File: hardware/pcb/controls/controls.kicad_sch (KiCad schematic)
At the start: 52 parts, among them J1 Conn_02x08_Odd_Even, J2 Conn_02x08_Odd_Even, J3 Conn_02x08_Odd_Even, J4 Conn_02x08_Odd_Even, SW1 SW_SPST, SW10 SW_SPST, SW11 SW_SPST, SW12 SW_SPST, SW2 SW_SPST, SW3 SW_SPST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

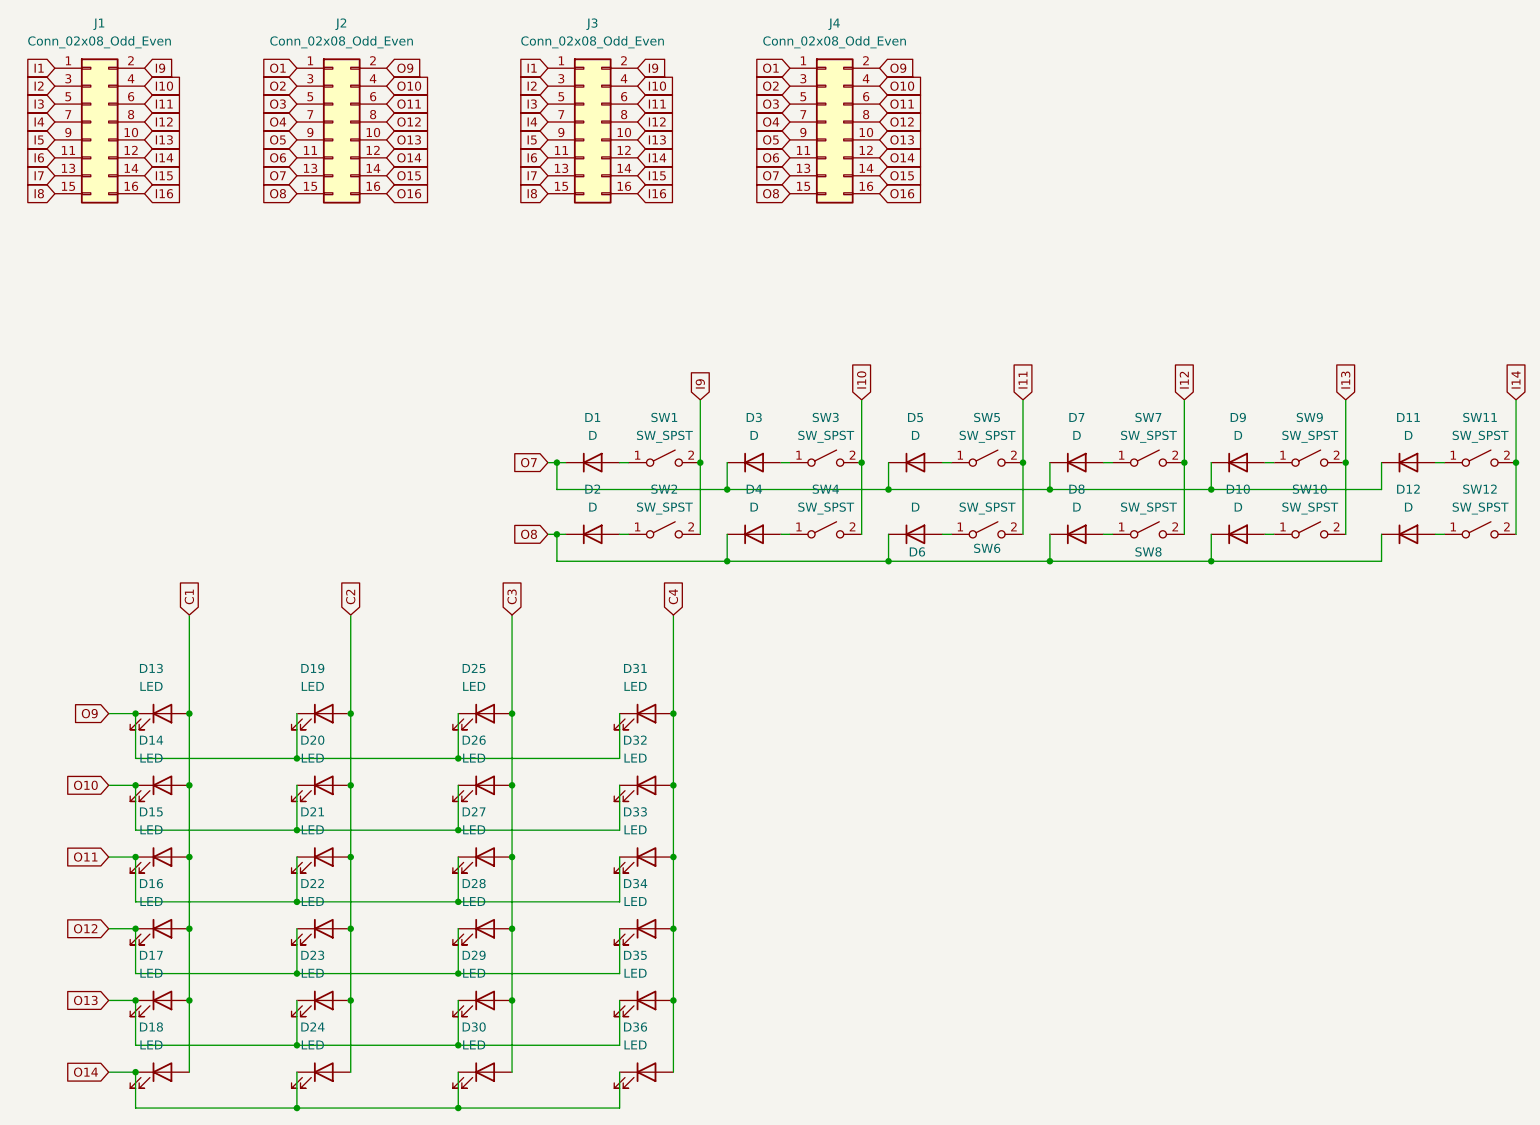
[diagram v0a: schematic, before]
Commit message: hardware: add schematics
add controls, io, keys, and nucleo hat boards
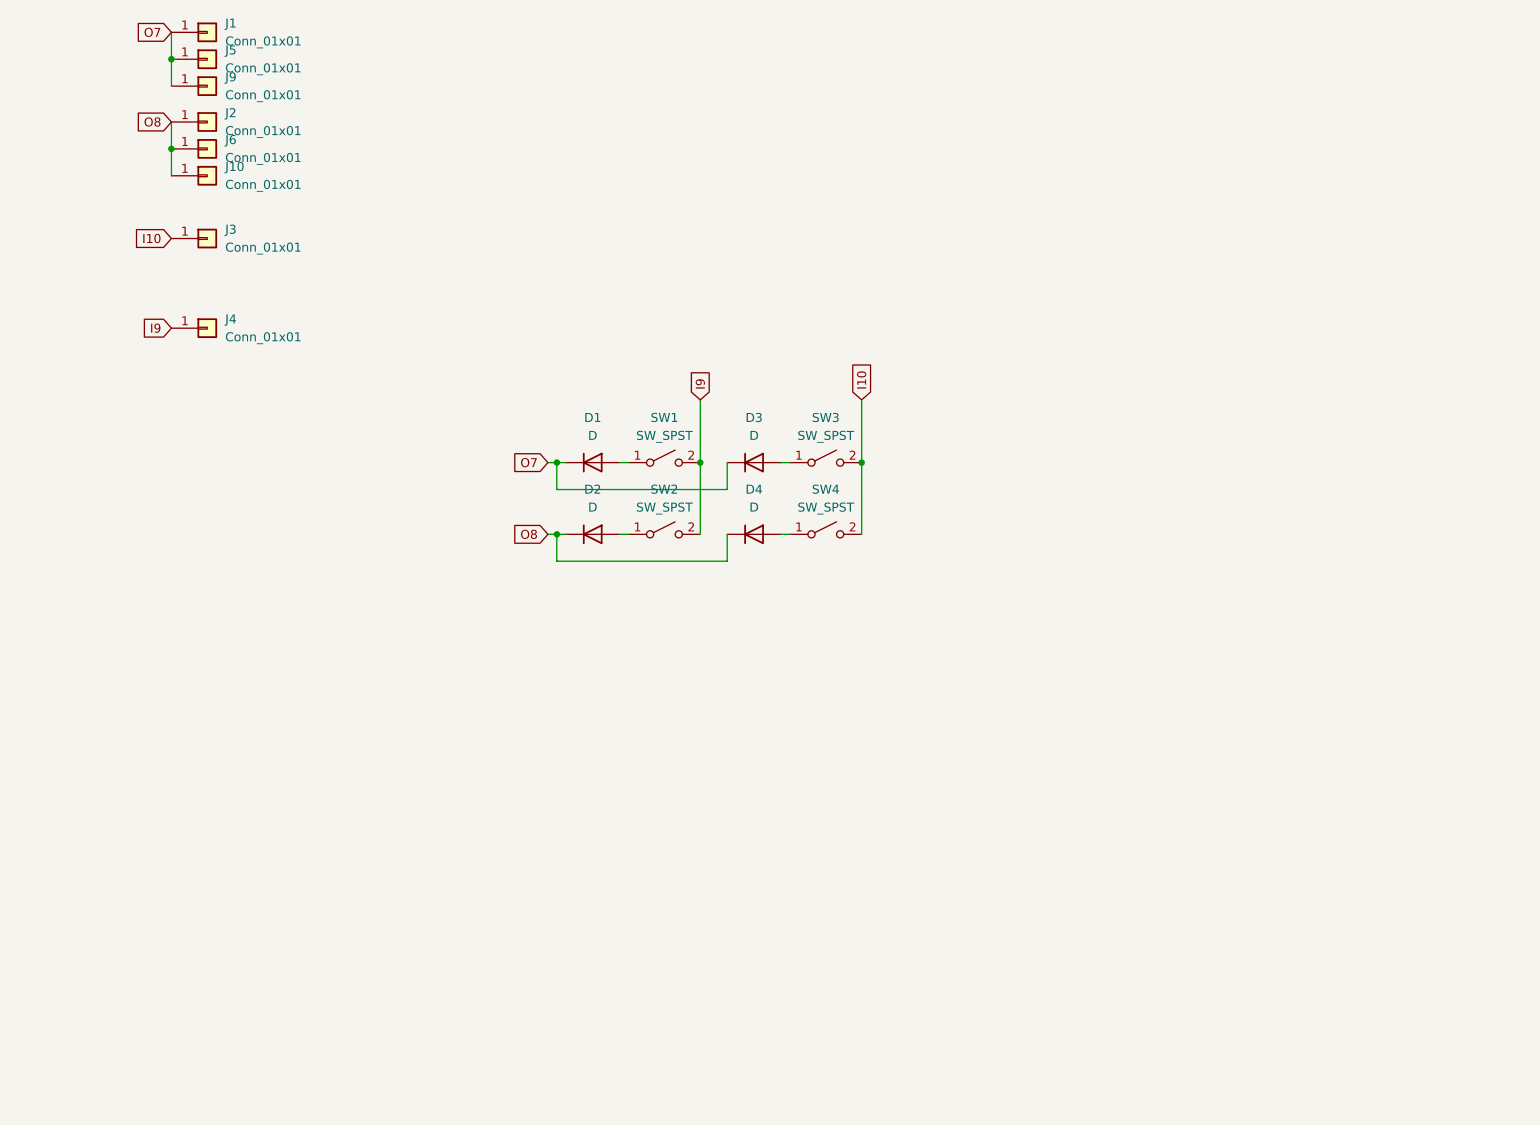
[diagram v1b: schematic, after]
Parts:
- removed D10, D11, D12, D5, D6, D7, D8, D9: D, Diode_THT:D_DO-35_SOD27_P7.62mm_Horizontal, symbol Device:D
- removed D13, D14, D15, D16, D17, D18, D19, D20, D21, D22, D23, D24, D25, D26, D27, D28, D29, D30, D31, D32, D33, D34, D35, D36: LED, LED_SMD:LED_0805_2012Metric, symbol Device:LED
- removed J1, J2, J3, J4: Conn_02x08_Odd_Even, Connector_PinHeader_1.27mm:PinHeader_2x08_P1.27mm_Vertical, symbol Connector_Generic:Conn_02x08_Odd_Even
- removed SW10, SW11, SW12, SW5, SW6, SW7, SW8, SW9: SW_SPST, Button_Switch_Keyboard:SW_Cherry_MX_1.00u_PCB, symbol Switch:SW_SPST
- added J1, J10, J2, J3, J4, J5, J6, J9: Conn_01x01, Connector_PinHeader_1.27mm:PinHeader_1x01_P1.27mm_Vertical, symbol Connector_Generic:Conn_01x01
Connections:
- net I10: now also J3.1 (Pin_1)
- net I9: now also J4.1 (Pin_1)
- net O7: now also J1.1 (Pin_1), J5.1 (Pin_1), J9.1 (Pin_1)
- net O8: now also J10.1 (Pin_1), J2.1 (Pin_1), J6.1 (Pin_1)
